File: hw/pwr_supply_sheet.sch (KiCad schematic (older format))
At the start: 15 parts

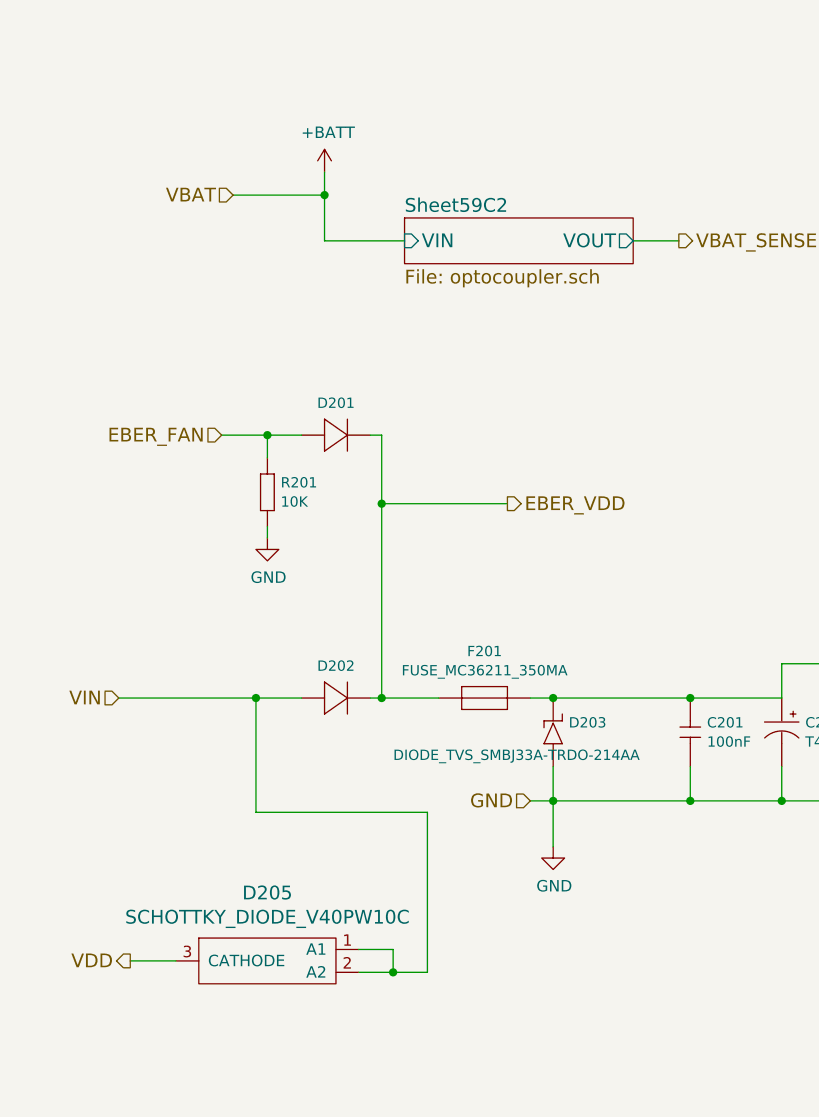
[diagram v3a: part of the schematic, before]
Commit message: heater shuts down when ignition key is turned off
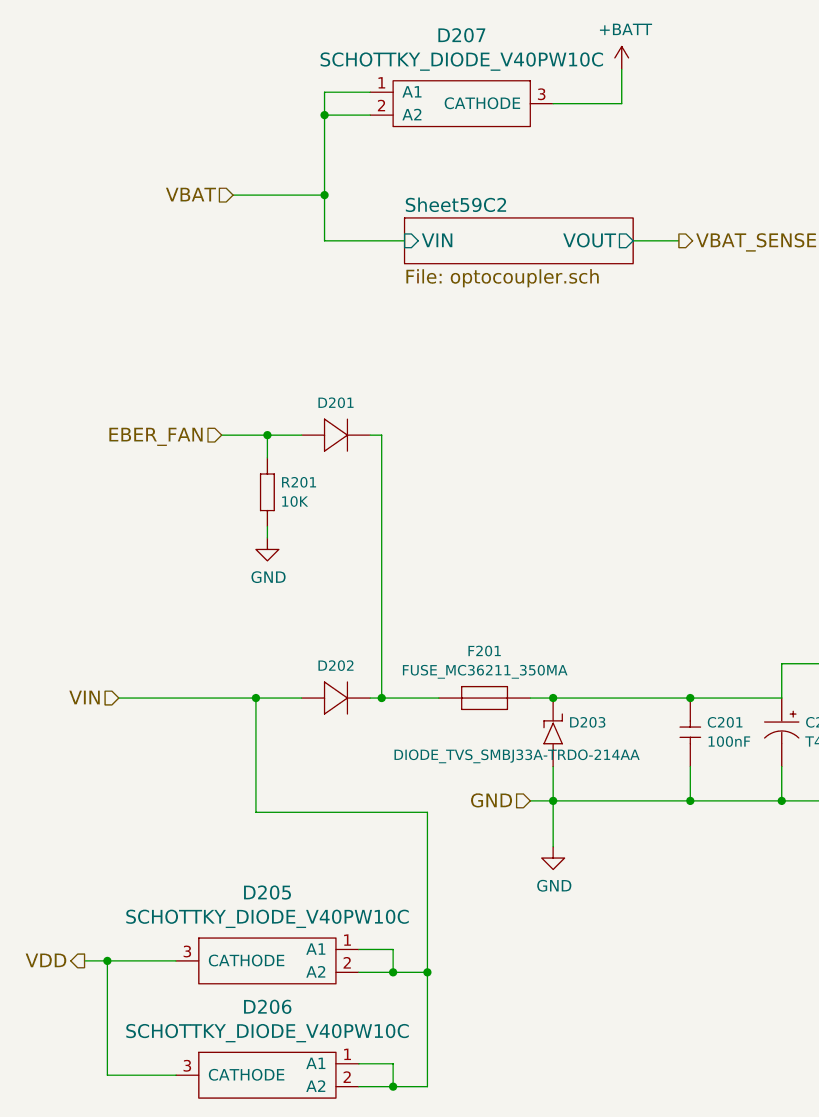
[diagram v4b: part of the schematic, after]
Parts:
- added D206, D207: SCHOTTKY_DIODE_V40PW10C, usevolt:SlimDPAK, symbol SCHOTTKY_DIODE_V40PW10C
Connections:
- net +BATT: now also D207.3 (CATHODE)
- net VDD: now also D206.3 (CATHODE)
- net VIN: now also D206.1 (A1), D206.2 (A2)
- net EBER_VDD: no longer names the net of D201.P$2 (N), D202.P$2 (N), F201.P$1
- new net VBAT: D207.1 (A1), D207.2 (A2)
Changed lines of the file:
@@
 EESchema Schematic File Version 2
+LIBS:fsb-rescue
 LIBS:kemet
 LIBS:power
@@
 $Descr A4 11693 8268
 encoding utf-8
-Sheet 2 9
+Sheet 2 6
 Title "Power supply"
 Date "2016-08-20"
@@
 	1    3400 3950
 	0    1    1    0
-$EndComp
-$Comp
-L LM2671SOIC8 VR201
-U 1 1 57B82261
-P 4850 4150
-F 0 "VR201" H 5050 4804 45  0000 C CNN
-F 1 "LM2671SOIC8" H 5050 4720 45  0000 C CNN
-F 2 "usevolt:SOIC8" H 4880 4300 20  0001 C CNN
-F 3 "http://www.farnell.com/datasheets/1902681.pdf?_ga=1.246738500.1948984246.1460023966" H 4650 4670 60  0001 C CNN
-F 4 "1469200" H 5050 5070 60  0001 C CNN "1st Source Part Number"
-F 5 "926-LM2671M-5.0/NOPB" H 5250 5270 60  0001 C CNN "2nd Source Part Number"
-F 6 "Farnell" H 4950 4970 60  0001 C CNN "1st Source"
-F 7 "LM2671M-5.0/NOPB" H 4850 4870 60  0001 C CNN "Manufacturer Part Number"
-F 8 "Mouser" H 5150 5170 60  0001 C CNN "2nd Source"
-F 9 "TEXAS INSTRUMENTS" H 4750 4770 60  0001 C CNN "Manufacturer"
-	1    4850 4150
-	1    0    0    -1
 $EndComp
 $Comp
@@
 	6850 3600 6850 3850
 $Comp
-L +5V #PWR07
+L +5V #PWR206
 U 1 1 57B831F8
 P 6850 3600
-F 0 "#PWR07" H 6850 3450 50  0001 C CNN
+F 0 "#PWR206" H 6850 3450 50  0001 C CNN
 F 1 "+5V" H 6865 3773 50  0000 C CNN
 F 2 "" H 6850 3600 50  0000 C CNN
@@
 Connection ~ 6850 3750
 $Comp
-L +3V3 #PWR08
+L +3V3 #PWR207
 U 1 1 57B83259
 P 8600 3600
-F 0 "#PWR08" H 8600 3450 50  0001 C CNN
+F 0 "#PWR207" H 8600 3450 50  0001 C CNN
 F 1 "+3V3" H 8615 3773 50  0000 C CNN
 F 2 "" H 8600 3600 50  0000 C CNN
@@
 Wire Wire Line
 	8750 3600 8600 3600
-Text HLabel 950  5000 0    60   Output ~ 0
+Text HLabel 750  5000 0    60   Output ~ 0
 VDD
 Text HLabel 2700 4300 0    60   Input ~ 0
@@
 NoConn ~ 4550 4050
 $Comp
-L VDD #PWR09
+L VDD #PWR204
 U 1 1 57B9C56A
 P 4250 2100
-F 0 "#PWR09" H 4250 1950 50  0001 C CNN
+F 0 "#PWR204" H 4250 1950 50  0001 C CNN
 F 1 "VDD" H 4267 2273 50  0000 C CNN
 F 2 "" H 4250 2100 50  0000 C CNN
@@
 $EndComp
 $Comp
-L PWR_FLAG #FLG010
+L PWR_FLAG #FLG201
 U 1 1 57B9C59C
 P 4250 2300
-F 0 "#FLG010" H 4250 2395 50  0001 C CNN
+F 0 "#FLG201" H 4250 2395 50  0001 C CNN
 F 1 "PWR_FLAG" H 4250 2523 50  0000 C CNN
 F 2 "" H 4250 2300 50  0000 C CNN
@@
 	4250 2300 4250 2100
 $Comp
-L GND #PWR011
+L GND #PWR205
 U 1 1 57B9D351
 P 4750 2350
-F 0 "#PWR011" H 4750 2100 50  0001 C CNN
+F 0 "#PWR205" H 4750 2100 50  0001 C CNN
 F 1 "GND" H 4755 2177 50  0000 C CNN
 F 2 "" H 4750 2350 50  0000 C CNN
@@
 $EndComp
 $Comp
-L PWR_FLAG #FLG012
+L PWR_FLAG #FLG202
 U 1 1 57B9D3A1
 P 4750 2150
-F 0 "#FLG012" H 4750 2245 50  0001 C CNN
+F 0 "#FLG202" H 4750 2245 50  0001 C CNN
 F 1 "PWR_FLAG" H 4750 2374 50  0000 C CNN
 F 2 "" H 4750 2150 50  0000 C CNN
@@
 	4750 2150 4750 2350
 $Comp
-L GND #PWR013
+L GND #PWR202
 U 1 1 57CF1F5E
 P 2800 4500
-F 0 "#PWR013" H 2800 4250 50  0001 C CNN
+F 0 "#PWR202" H 2800 4250 50  0001 C CNN
 F 1 "GND" H 2805 4327 50  0000 C CNN
 F 2 "" H 2800 4500 50  0000 C CNN
@@
 	3800 3850 3800 3700
 Wire Wire Line
-	950  5000 1150 5000
+	750  5000 1150 5000
 Connection ~ 1500 3850
 Wire Wire Line
@@
 VBAT
 $Comp
-L +BATT #PWR014
+L +BATT #PWR203
 U 1 1 5988E784
-P 1800 1550
-F 0 "#PWR014" H 1800 1400 50  0001 C CNN
-F 1 "+BATT" H 1815 1723 50  0000 C CNN
-F 2 "" H 1800 1550 50  0000 C CNN
-F 3 "" H 1800 1550 50  0000 C CNN
-	1    1800 1550
-	1    0    0    -1
-$EndComp
-Wire Wire Line
-	1800 1550 1800 1850
+P 3100 1100
+F 0 "#PWR203" H 3100 950 50  0001 C CNN
+F 1 "+BATT" H 3115 1273 50  0000 C CNN
+F 2 "" H 3100 1100 50  0000 C CNN
+F 3 "" H 3100 1100 50  0000 C CNN
+	1    3100 1100
+	1    0    0    -1
+$EndComp
+Wire Wire Line
+	1800 1200 1800 1850
 Wire Wire Line
 	1800 1650 1400 1650
@@
 Connection ~ 1550 2700
 $Comp
-L GND #PWR015
+L GND #PWR201
 U 1 1 5988FF98
 P 1550 3150
-F 0 "#PWR015" H 1550 2900 50  0001 C CNN
+F 0 "#PWR201" H 1550 2900 50  0001 C CNN
 F 1 "GND" H 1555 2977 50  0000 C CNN
 F 2 "" H 1550 3150 50  0000 C CNN
@@
 	1950 5050 2250 5050
 Wire Wire Line
-	2250 5050 2250 4350
+	2250 4350 2250 5550
 Wire Wire Line
 	2250 4350 1500 4350
@@
 	2100 4950 2100 5050
 Connection ~ 2100 5050
-Text HLabel 2600 3000 2    60   Output ~ 0
-EBER_VDD
-Wire Wire Line
-	2050 3000 2600 3000
-Connection ~ 2050 3000
+Wire Wire Line
+	1800 1850 2150 1850
+Wire Wire Line
+	3150 1850 3350 1850
+$Comp
+L SCHOTTKY_DIODE_V40PW10C D206
+U 1 1 5A05E274
+P 1550 5550
+F 0 "D206" H 1550 5897 60  0000 C CNN
+F 1 "SCHOTTKY_DIODE_V40PW10C" H 1550 5791 60  0000 C CNN
+F 2 "usevolt:SlimDPAK" H 1350 5200 60  0001 C CNN
+F 3 "http://www.farnell.com/datasheets/2245239.pdf?_ga=2.16591231.874534928.1505194133-1862443086.1504075057" H 1350 5200 60  0001 C CNN
+F 4 "2535169" H 1900 6150 60  0001 C CNN "1st Source Part Number"
+F 5 "Digikey" H 2000 6250 60  0001 C CNN "2nd Source"
+F 6 "Farnell" H 1800 6050 60  0001 C CNN "1st Source"
+F 7 "V40PW10CHM3/I" H 1700 5950 60  0001 C CNN "Manufacturer Part Number"
+F 8 "V40PW10CHM3/IGICT-ND" H 2100 6350 60  0001 C CNN "2nd Source Part Number"
+F 9 "VISHAY" H 1600 5850 60  0001 C CNN "Manufacturer"
+	1    1550 5550
+	-1   0    0    -1
+$EndComp
+Wire Wire Line
+	1150 5500 850  5500
+Wire Wire Line
+	850  5500 850  5000
+Connection ~ 850  5000
+Wire Wire Line
+	2250 5550 1950 5550
+Connection ~ 2250 5050
+Wire Wire Line
+	1950 5450 2100 5450
+Wire Wire Line
+	2100 5450 2100 5550
+Connection ~ 2100 5550
+$Comp
+L LM2671SOIC8 VR201
+U 1 1 5A060F27
+P 4850 4150
+F 0 "VR201" H 5050 4804 45  0000 C CNN
+F 1 "LM2671SOIC8" H 5050 4720 45  0000 C CNN
+F 2 "usevolt:SOIC8" H 4880 4300 20  0001 C CNN
+F 3 "http://www.farnell.com/datasheets/1902681.pdf?_ga=1.246738500.1948984246.1460023966" H 4650 4670 60  0001 C CNN
+F 4 "1469200" H 5050 5070 60  0001 C CNN "1st Source Part Number"
+F 5 "926-LM2671M-5.0/NOPB" H 5250 5270 60  0001 C CNN "2nd Source Part Number"
+F 6 "Farnell" H 4950 4970 60  0001 C CNN "1st Source"
+F 7 "LM2671M-5.0/NOPB" H 4850 4870 60  0001 C CNN "Manufacturer Part Number"
+F 8 "Mouser" H 5150 5170 60  0001 C CNN "2nd Source"
+F 9 "TEXAS INSTRUMENTS" H 4750 4770 60  0001 C CNN "Manufacturer"
+	1    4850 4150
+	1    0    0    -1
+$EndComp
 $Sheet
 S 2150 1750 1000 200
@@
 F3 "VIN" I L 2150 1850 60
 $EndSheet
-Wire Wire Line
-	1800 1850 2150 1850
-Wire Wire Line
-	3150 1850 3350 1850
+$Comp
+L SCHOTTKY_DIODE_V40PW10C D207
+U 1 1 5A081648
+P 2400 1300
+F 0 "D207" H 2400 1647 60  0000 C CNN
+F 1 "SCHOTTKY_DIODE_V40PW10C" H 2400 1541 60  0000 C CNN
+F 2 "usevolt:SlimDPAK" H 2200 950 60  0001 C CNN
+F 3 "http://www.farnell.com/datasheets/2245239.pdf?_ga=2.16591231.874534928.1505194133-1862443086.1504075057" H 2200 950 60  0001 C CNN
+F 4 "2535169" H 2750 1900 60  0001 C CNN "1st Source Part Number"
+F 5 "Digikey" H 2850 2000 60  0001 C CNN "2nd Source"
+F 6 "Farnell" H 2650 1800 60  0001 C CNN "1st Source"
+F 7 "V40PW10CHM3/I" H 2550 1700 60  0001 C CNN "Manufacturer Part Number"
+F 8 "V40PW10CHM3/IGICT-ND" H 2950 2100 60  0001 C CNN "2nd Source Part Number"
+F 9 "VISHAY" H 2450 1600 60  0001 C CNN "Manufacturer"
+	1    2400 1300
+	1    0    0    -1
+$EndComp
+Wire Wire Line
+	1800 1300 2000 1300
+Wire Wire Line
+	2000 1200 1800 1200
+Connection ~ 1800 1300
+Wire Wire Line
+	2800 1250 3100 1250
+Wire Wire Line
+	3100 1250 3100 1100
 $EndSCHEMATC

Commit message: hw 2.1.0 created, not yet ordered
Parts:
- removed C202: T491D226K035AT, kemet:7343, symbol T491D226K035AT
- removed R201: 10K, multicomp:0603, symbol 10K
- added C202: CAP_EEE-FK1H470P, usevolt:CAP_EEE-FK1H470P, symbol CAP_EEE-FK1H470P
- added D208: DIODE_TVS_TPSMD28A, usevolt:DO-214AB, symbol DIODE_TVS_TPSMD28A
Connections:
- net GND: now also C202.-, D208.1 (P)
- net VDD: now also D208.2 (N)
- net at C201.1 (C1), D203.P$2 (N), F201.P$2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: now also C202.+
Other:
- moved on the sheet: D205, D206
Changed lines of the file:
@@
-$EndComp
-$Comp
-L DIODE_TVS_SMBJ33A-TRDO-214AA D203
-U 1 1 57B820C1
-P 2800 4050
-F 0 "D203" V 2892 3982 45  0000 R CNN
-F 1 "DIODE_TVS_SMBJ33A-TRDO-214AA" V 2750 4750 45  0000 R CNN
-F 2 "usevolt:DO-214AA" H 2830 4200 20  0001 C CNN
-F 3 "http://www.littelfuse.com/~/media/electronics/datasheets/tvs_diodes/littelfuse_tvs_diode_smbj_datasheet.pdf.pdf" H 2910 4060 60  0001 C CNN
-F 4 "Digi-Key" H 3210 4360 60  0001 C CNN "1st Source"
-F 5 "Littlefuse" H 3010 4160 60  0001 C CNN "Manufacturer"
-F 6 "SMBJ33A" H 3110 4260 60  0001 C CNN "Manufacturer Part Number"
-F 7 "SMBJ33ALFCT-ND" H 3310 4460 60  0001 C CNN "1st Source Part Number"
-	1    2800 4050
-	0    -1   -1   0
 $EndComp
 $Comp
@@
 	900  3850 1700 3850
 Wire Wire Line
-	3800 3700 4550 3700
-Wire Wire Line
-	4550 3700 4550 3750
+	3800 3750 4550 3750
 Text HLabel 7050 3600 2    60   Output ~ 0
 +5V
@@
 Wire Wire Line
 	8750 3600 8600 3600
-Text HLabel 750  5000 0    60   Output ~ 0
+Text HLabel 750  5200 0    60   Output ~ 0
 VDD
 Text HLabel 2700 4300 0    60   Input ~ 0
@@
 $EndComp
 Wire Wire Line
-	3800 3850 3800 3700
-Wire Wire Line
-	750  5000 1150 5000
+	3800 3850 3800 3750
+Wire Wire Line
+	750  5200 1900 5200
 Connection ~ 1500 3850
 Wire Wire Line
@@
 	0    1    1    0
 $EndComp
-$Comp
-L T491D226K035AT C202
-U 1 1 58946146
-P 3800 4050
-F 0 "C202" V 3708 4153 45  0000 L CNN
-F 1 "T491D226K035AT" V 3792 4153 45  0000 L CNN
-F 2 "kemet:7343" H 3830 4200 20  0001 C CNN
-F 3 "http://www.farnell.com/datasheets/2121523.pdf?_ga=1.259966538.1948984246.1460023966" H 3800 3990 60  0001 C CNN
-F 4 "399-8375-1-ND" H 4400 4590 60  0001 C CNN "2nd Source Part Number"
-F 5 "Farnell" H 4100 4290 60  0001 C CNN "1st Source"
-F 6 "T491D226K035AT" H 4000 4190 60  0001 C CNN "Manufacturer Part Number"
-F 7 "Digikey" H 4300 4490 60  0001 C CNN "2nd Source"
-F 8 "Kemet" H 3900 4090 60  0001 C CNN "Manufacturer"
-F 9 "1457504" H 4200 4390 60  0001 C CNN "1st Source Part Number"
-	1    3800 4050
-	0    1    1    0
-$EndComp
 Wire Wire Line
 	2000 3850 2300 3850
@@
 	2050 2700 2050 3850
 Connection ~ 2050 3850
-$Comp
-L 10K R201
-U 1 1 5988FEDF
-P 1550 2900
-F 0 "R201" V 1558 2958 45  0000 L CNN
-F 1 "10K" V 1642 2958 45  0000 L CNN
-F 2 "multicomp:0603" H 1580 3050 20  0001 C CNN
-F 3 "http://www.farnell.com/datasheets/1788326.pdf?_ga=1.214208087.1948984246.1460023966" H 1519 2939 60  0001 C CNN
-F 4 "9330399" H 1919 3339 60  0001 C CNN "1st Source Part Number"
-F 5 "Farnell" H 1819 3239 60  0001 C CNN "1st Source"
-F 6 "MC0063W0603110K" H 1719 3139 60  0001 C CNN "Manufacturer Part Number"
-F 7 "MULTICOMP" H 1619 3039 60  0001 C CNN "Manufacturer"
-	1    1550 2900
-	0    1    1    0
-$EndComp
-Connection ~ 1550 2700
-$Comp
-L GND #PWR201
-U 1 1 5988FF98
-P 1550 3150
-F 0 "#PWR201" H 1550 2900 50  0001 C CNN
-F 1 "GND" H 1555 2977 50  0000 C CNN
-F 2 "" H 1550 3150 50  0000 C CNN
-F 3 "" H 1550 3150 50  0000 C CNN
-	1    1550 3150
-	1    0    0    -1
-$EndComp
-Wire Wire Line
-	1550 3150 1550 3100
-Wire Wire Line
-	1550 2700 1550 2800
 Connection ~ 1800 1650
 Text HLabel 3350 1850 2    60   Output ~ 0
@@
 L SCHOTTKY_DIODE_V40PW10C D205
 U 1 1 59C29BB6
-P 1550 5050
-F 0 "D205" H 1550 5397 60  0000 C CNN
-F 1 "SCHOTTKY_DIODE_V40PW10C" H 1550 5291 60  0000 C CNN
-F 2 "usevolt:SlimDPAK" H 1350 4700 60  0001 C CNN
-F 3 "http://www.farnell.com/datasheets/2245239.pdf?_ga=2.16591231.874534928.1505194133-1862443086.1504075057" H 1350 4700 60  0001 C CNN
-F 4 "2535169" H 1900 5650 60  0001 C CNN "1st Source Part Number"
-F 5 "Digikey" H 2000 5750 60  0001 C CNN "2nd Source"
-F 6 "Farnell" H 1800 5550 60  0001 C CNN "1st Source"
-F 7 "V40PW10CHM3/I" H 1700 5450 60  0001 C CNN "Manufacturer Part Number"
-F 8 "V40PW10CHM3/IGICT-ND" H 2100 5850 60  0001 C CNN "2nd Source Part Number"
-F 9 "VISHAY" H 1600 5350 60  0001 C CNN "Manufacturer"
-	1    1550 5050
+P 2300 5250
+F 0 "D205" H 2300 5597 60  0000 C CNN
+F 1 "SCHOTTKY_DIODE_V40PW10C" H 2300 5491 60  0000 C CNN
+F 2 "usevolt:SlimDPAK" H 2100 4900 60  0001 C CNN
+F 3 "http://www.farnell.com/datasheets/2245239.pdf?_ga=2.16591231.874534928.1505194133-1862443086.1504075057" H 2100 4900 60  0001 C CNN
+F 4 "2535169" H 2650 5850 60  0001 C CNN "1st Source Part Number"
+F 5 "Digikey" H 2750 5950 60  0001 C CNN "2nd Source"
+F 6 "Farnell" H 2550 5750 60  0001 C CNN "1st Source"
+F 7 "V40PW10CHM3/I" H 2450 5650 60  0001 C CNN "Manufacturer Part Number"
+F 8 "V40PW10CHM3/IGICT-ND" H 2850 6050 60  0001 C CNN "2nd Source Part Number"
+F 9 "VISHAY" H 2350 5550 60  0001 C CNN "Manufacturer"
+	1    2300 5250
 	-1   0    0    -1
 $EndComp
 Wire Wire Line
-	1950 5050 2250 5050
-Wire Wire Line
-	2250 4350 2250 5550
-Wire Wire Line
-	2250 4350 1500 4350
-Wire Wire Line
-	1500 4350 1500 3850
-Wire Wire Line
-	1950 4950 2100 4950
-Wire Wire Line
-	2100 4950 2100 5050
-Connection ~ 2100 5050
+	2700 5250 3000 5250
+Wire Wire Line
+	3000 5750 3000 4800
+Wire Wire Line
+	3000 4800 1500 4800
+Wire Wire Line
+	1500 4800 1500 3850
+Wire Wire Line
+	2700 5150 2850 5150
+Wire Wire Line
+	2850 5150 2850 5250
+Connection ~ 2850 5250
 Wire Wire Line
 	1800 1850 2150 1850
@@
 L SCHOTTKY_DIODE_V40PW10C D206
 U 1 1 5A05E274
-P 1550 5550
-F 0 "D206" H 1550 5897 60  0000 C CNN
-F 1 "SCHOTTKY_DIODE_V40PW10C" H 1550 5791 60  0000 C CNN
-F 2 "usevolt:SlimDPAK" H 1350 5200 60  0001 C CNN
-F 3 "http://www.farnell.com/datasheets/2245239.pdf?_ga=2.16591231.874534928.1505194133-1862443086.1504075057" H 1350 5200 60  0001 C CNN
-F 4 "2535169" H 1900 6150 60  0001 C CNN "1st Source Part Number"
-F 5 "Digikey" H 2000 6250 60  0001 C CNN "2nd Source"
-F 6 "Farnell" H 1800 6050 60  0001 C CNN "1st Source"
-F 7 "V40PW10CHM3/I" H 1700 5950 60  0001 C CNN "Manufacturer Part Number"
-F 8 "V40PW10CHM3/IGICT-ND" H 2100 6350 60  0001 C CNN "2nd Source Part Number"
-F 9 "VISHAY" H 1600 5850 60  0001 C CNN "Manufacturer"
-	1    1550 5550
+P 2300 5750
+F 0 "D206" H 2300 6097 60  0000 C CNN
+F 1 "SCHOTTKY_DIODE_V40PW10C" H 2300 5991 60  0000 C CNN
+F 2 "usevolt:SlimDPAK" H 2100 5400 60  0001 C CNN
+F 3 "http://www.farnell.com/datasheets/2245239.pdf?_ga=2.16591231.874534928.1505194133-1862443086.1504075057" H 2100 5400 60  0001 C CNN
+F 4 "2535169" H 2650 6350 60  0001 C CNN "1st Source Part Number"
+F 5 "Digikey" H 2750 6450 60  0001 C CNN "2nd Source"
+F 6 "Farnell" H 2550 6250 60  0001 C CNN "1st Source"
+F 7 "V40PW10CHM3/I" H 2450 6150 60  0001 C CNN "Manufacturer Part Number"
+F 8 "V40PW10CHM3/IGICT-ND" H 2850 6550 60  0001 C CNN "2nd Source Part Number"
+F 9 "VISHAY" H 2350 6050 60  0001 C CNN "Manufacturer"
+	1    2300 5750
 	-1   0    0    -1
 $EndComp
 Wire Wire Line
-	1150 5500 850  5500
-Wire Wire Line
-	850  5500 850  5000
-Connection ~ 850  5000
-Wire Wire Line
-	2250 5550 1950 5550
-Connection ~ 2250 5050
-Wire Wire Line
-	1950 5450 2100 5450
-Wire Wire Line
-	2100 5450 2100 5550
-Connection ~ 2100 5550
+	1900 5700 1650 5700
+Wire Wire Line
+	1650 5700 1650 5200
+Connection ~ 1650 5200
+Wire Wire Line
+	2700 5750 3000 5750
+Connection ~ 3000 5250
+Wire Wire Line
+	2700 5650 2850 5650
+Wire Wire Line
+	2850 5650 2850 5750
+Connection ~ 2850 5750
 $Comp
 L LM2671SOIC8 VR201
@@
 Wire Wire Line
 	3100 1250 3100 1100
+$Comp
+L DIODE_TVS_TPSMD28A D208
+U 1 1 5A0E2A07
+P 850 5500
+F 0 "D208" V 942 5432 45  0000 R CNN
+F 1 "DIODE_TVS_TPSMD28A" V 858 5432 45  0000 R CNN
+F 2 "usevolt:DO-214AB" H 880 5650 20  0001 C CNN
+F 3 "http://www.littelfuse.com/~/media/electronics/datasheets/tvs_diodes/littelfuse_tvs_diode_tpsmd_datasheet.pdf.pdf" H 960 5510 60  0001 C CNN
+F 4 "Digi-Key" H 1260 5810 60  0001 C CNN "1st Source"
+F 5 "Littlefuse" H 1060 5610 60  0001 C CNN "Manufacturer"
+F 6 "TPSMD28A" H 1160 5710 60  0001 C CNN "Manufacturer Part Number"
+F 7 "F6570CT-ND" H 1360 5910 60  0001 C CNN "1st Source Part Number"
+	1    850  5500
+	0    -1   -1   0
+$EndComp
+Wire Wire Line
+	850  5300 850  5200
+Connection ~ 850  5200
+$Comp
+L GND #PWR201
+U 1 1 5A0E2B45
+P 850 5850
+F 0 "#PWR201" H 850 5600 50  0001 C CNN
+F 1 "GND" H 855 5677 50  0000 C CNN
+F 2 "" H 850 5850 50  0000 C CNN
+F 3 "" H 850 5850 50  0000 C CNN
+	1    850  5850
+	1    0    0    -1
+$EndComp
+Wire Wire Line
+	850  5850 850  5600
+$Comp
+L DIODE_TVS_SMBJ33A-TRDO-214AA D203
+U 1 1 57B820C1
+P 2800 4050
+F 0 "D203" V 2892 3982 45  0000 R CNN
+F 1 "DIODE_TVS_SMBJ33A-TRDO-214AA" V 2750 4750 45  0000 R CNN
+F 2 "usevolt:DO-214AA" H 2830 4200 20  0001 C CNN
+F 3 "http://www.littelfuse.com/~/media/electronics/datasheets/tvs_diodes/littelfuse_tvs_diode_smbj_datasheet.pdf.pdf" H 2910 4060 60  0001 C CNN
+F 4 "Digi-Key" H 3210 4360 60  0001 C CNN "1st Source"
+F 5 "Littlefuse" H 3010 4160 60  0001 C CNN "Manufacturer"
+F 6 "SMBJ33A" H 3110 4260 60  0001 C CNN "Manufacturer Part Number"
+F 7 "SMBJ33ALFCT-ND" H 3310 4460 60  0001 C CNN "1st Source Part Number"
+	1    2800 4050
+	0    -1   -1   0
+$EndComp
+$Comp
+L CAP_EEE-FK1H470P C202
+U 1 1 5A0E34C5
+P 3800 4050
+F 0 "C202" V 3708 4153 45  0000 L CNN
+F 1 "CAP_EEE-FK1H470P" V 3792 4153 45  0000 L CNN
+F 2 "usevolt:CAP_EEE-FK1H470P" H 3830 4200 20  0001 C CNN
+F 3 "http://industrial.panasonic.com/www-cgi/jvcr13pz.cgi?E+PZ+3+ABA0120+EEEFK1H470P+7+WW" H 3800 3990 60  0001 C CNN
+F 4 "667-EEE-FK1H470P" H 4400 4590 60  0001 C CNN "2nd Source Part Number"
+F 5 "Digi-Key" H 4100 4290 60  0001 C CNN "1st Source"
+F 6 "EEE-FK1H470P" H 4000 4190 60  0001 C CNN "Manufacturer Part Number"
+F 7 "Mouser" H 4300 4490 60  0001 C CNN "2nd Source"
+F 8 "Panasonic Electronic Components" H 3900 4090 60  0001 C CNN "Manufacturer"
+F 9 "PCE3815CT-ND" H 4200 4390 60  0001 C CNN "1st Source Part Number"
+	1    3800 4050
+	0    1    1    0
+$EndComp
+Connection ~ 3800 3850
 $EndSCHEMATC
